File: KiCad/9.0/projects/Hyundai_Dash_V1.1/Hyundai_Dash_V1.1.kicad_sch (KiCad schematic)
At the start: 30 parts, among them J1 +12V-GND, J10 GND-Fuel, J2 IGN-HS1-HS2-LS1-LS2, J3 C-CAN, J4 C-CAN, J5 C-CAN SPI, J6 B-CAN, J7 B-CAN, J8 B-CAN SPI, J9 Jumper Holder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

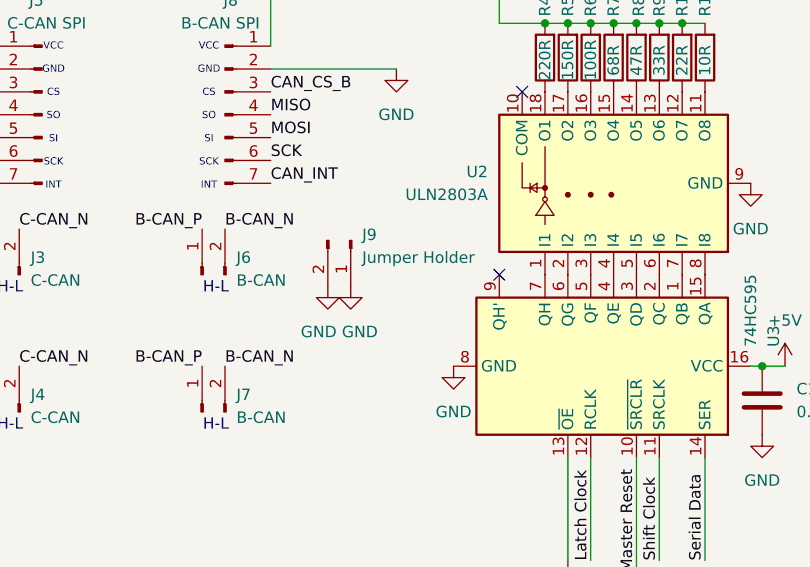
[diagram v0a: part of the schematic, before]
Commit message: KiCad: Hyundai_Dash_V1.1: remove jumper holder
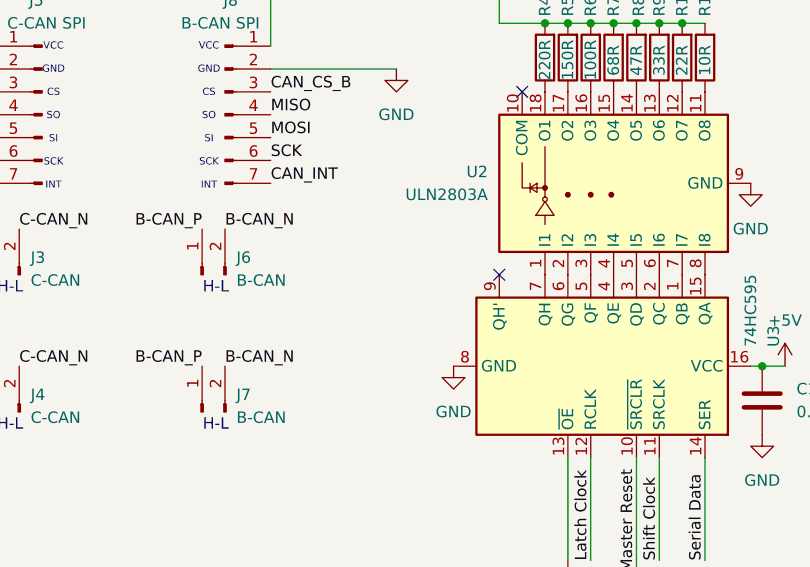
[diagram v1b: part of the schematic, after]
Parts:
- removed J9: Jumper Holder, Connector_PinHeader_2.54mm:PinHeader_1x02_P2.54mm_Vertical, symbol Connector:Conn_01x02_Pin
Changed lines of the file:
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@@
-	)
-	(symbol
-		(lib_id "power:GND")
-		(at 179.07 86.36 0)
-		(unit 1)
-		(exclude_from_sim no)
-		(in_bom yes)
-		(on_board yes)
-		(dnp no)
-		(property "Reference" "#PWR010"
-			(at 179.07 92.71 0)
-			(effects
-				(font
-					(size 1.27 1.27)
-				)
-				(hide yes)
-			)
-		)
-		(property "Value" "GND"
-			(at 180.086 91.44 0)
-			(effects
-				(font
-					(size 1.27 1.27)
-				)
-			)
-		)
-		(property "Footprint" ""
-			(at 179.07 86.36 0)
-			(effects
-				(font
-					(size 1.27 1.27)
-				)
-				(hide yes)
-			)
-		)
-		(property "Datasheet" ""
-			(at 179.07 86.36 0)
-			(effects
-				(font
-					(size 1.27 1.27)
-				)
-				(hide yes)
-			)
-		)
-		(property "Description" "Power symbol creates a global label with name \"GND\" , ground"
-			(at 179.07 86.36 0)
-			(effects
-				(font
-					(size 1.27 1.27)
-				)
-				(hide yes)
-			)
-		)
-		(pin "1"
-		)
-		(instances
-			(project "Kia_Dash_V1"
-				(path "/37058ee5-1984-4ba0-87f5-ec991eadee3c"
-					(reference "#PWR010")
-					(unit 1)
-				)
-			)
-		)
 	)
 	(symbol
@@
 	)
 	(symbol
-		(lib_id "power:GND")
-		(at 176.53 86.36 0)
-		(unit 1)
-		(exclude_from_sim no)
-		(in_bom yes)
-		(on_board yes)
-		(dnp no)
-		(property "Reference" "#PWR09"
-			(at 176.53 92.71 0)
-			(effects
-				(font
-					(size 1.27 1.27)
-				)
-				(hide yes)
-			)
-		)
-		(property "Value" "GND"
-			(at 175.514 91.44 0)
-			(effects
-				(font
-					(size 1.27 1.27)
-				)
-			)
-		)
-		(property "Footprint" ""
-			(at 176.53 86.36 0)
-			(effects
-				(font
-					(size 1.27 1.27)
-				)
-				(hide yes)
-			)
-		)
-		(property "Datasheet" ""
-			(at 176.53 86.36 0)
-			(effects
-				(font
-					(size 1.27 1.27)
-				)
-				(hide yes)
-			)
-		)
-		(property "Description" "Power symbol creates a global label with name \"GND\" , ground"
-			(at 176.53 86.36 0)
-			(effects
-				(font
-					(size 1.27 1.27)
-				)
-				(hide yes)
-			)
-		)
-		(pin "1"
-		)
-		(instances
-			(project "Kia_Dash_V1"
-				(path "/37058ee5-1984-4ba0-87f5-ec991eadee3c"
-					(reference "#PWR09")
-					(unit 1)
-				)
-			)
-		)
-	)
-	(symbol
 		(lib_id "Transistor_Array:ULN2803A")
 		(at 104.14 86.36 90)
@@
 					(unit 1)
 				)
-			)
-		)
-	)
-	(symbol
-		(lib_id "Connector:Conn_01x02_Pin")
-		(at 179.07 81.28 270)
-		(unit 1)
-		(exclude_from_sim no)
-		(in_bom no)
-		(on_board yes)
-		(dnp no)
-		(fields_autoplaced yes)
-		(property "Reference" "J9"
-			(at 180.34 80.6449 90)
-			(effects
-				(font
-					(size 1.27 1.27)
-				)
-				(justify left)
-			)
-		)
-		(property "Value" "Jumper Holder"
-			(at 180.34 83.1849 90)
-			(effects
-				(font
-					(size 1.27 1.27)
-				)
-				(justify left)
-			)
-		)
-		(property "Footprint" "Connector_PinHeader_2.54mm:PinHeader_1x02_P2.54mm_Vertical"
-			(at 179.07 81.28 0)
-			(effects
-				(font
-					(size 1.27 1.27)
-				)
-				(hide yes)
-			)
-		)
-		(property "Datasheet" "~"
-			(at 179.07 81.28 0)
-			(effects
-				(font
-					(size 1.27 1.27)
-				)
-				(hide yes)
-			)
-		)
-		(property "Description" "Generic connector, single row, 01x02, script generated"
-			(at 179.07 81.28 0)
-			(effects
-				(font
-					(size 1.27 1.27)
-				)
-				(hide yes)
-			)
-		)
-		(pin "1"
-		)
-		(pin "2"
-		)
-		(instances
-			(project "Hyundai_Dash_V3"
-				(path "/37058ee5-1984-4ba0-87f5-ec991eadee3c"
-					(reference "J9")
-					(unit 1)
-				)

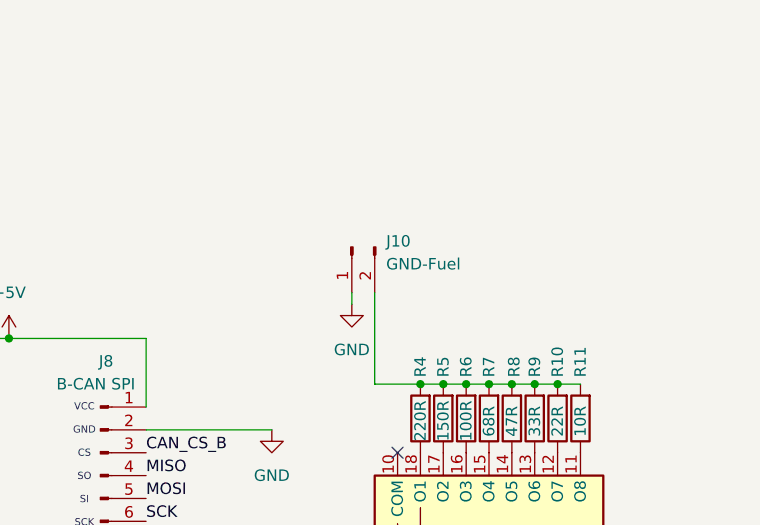
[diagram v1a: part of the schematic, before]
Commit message: KiCad: Hyundai_Dash_V1.1: reassign annotations
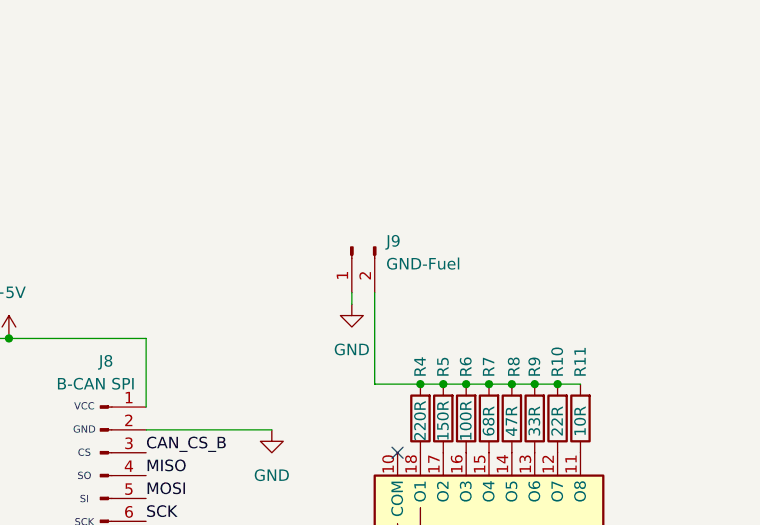
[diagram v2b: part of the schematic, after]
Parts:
- renumbered J10 to J9
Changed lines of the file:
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@@
 		(dnp no)
 		(fields_autoplaced yes)
-		(property "Reference" "#PWR014"
+		(property "Reference" "#PWR012"
 			(at 203.2 123.19 0)
 			(effects
@@
 			(project "Elantra_Nano"
 				(path "/37058ee5-1984-4ba0-87f5-ec991eadee3c"
-					(reference "#PWR014")
+					(reference "#PWR012")
 					(unit 1)
 				)
@@
 		(dnp no)
 		(fields_autoplaced yes)
-		(property "Reference" "J10"
+		(property "Reference" "J9"
 			(at 196.85 41.2749 90)
 			(effects
@@
 			(project "Elantra_Nano"
 				(path "/37058ee5-1984-4ba0-87f5-ec991eadee3c"
-					(reference "J10")
+					(reference "J9")
 					(unit 1)
 				)
@@
 		(dnp no)
 		(fields_autoplaced yes)
-		(property "Reference" "#PWR017"
+		(property "Reference" "#PWR015"
 			(at 227.33 99.06 0)
 			(effects
@@
 			(project "Elantra_Nano"
 				(path "/37058ee5-1984-4ba0-87f5-ec991eadee3c"
-					(reference "#PWR017")
+					(reference "#PWR015")
 					(unit 1)
 				)
@@
 		(dnp no)
 		(fields_autoplaced yes)
-		(property "Reference" "#PWR013"
+		(property "Reference" "#PWR011"
 			(at 193.04 54.61 0)
 			(effects
@@
 			(project "Elantra_Nano"
 				(path "/37058ee5-1984-4ba0-87f5-ec991eadee3c"
-					(reference "#PWR013")
+					(reference "#PWR011")
 					(unit 1)
 				)
@@
 		(dnp no)
 		(fields_autoplaced yes)
-		(property "Reference" "#PWR011"
+		(property "Reference" "#PWR09"
 			(at 184.15 68.58 0)
 			(effects
@@
 			(project "Hyundai_Dash_V3"
 				(path "/37058ee5-1984-4ba0-87f5-ec991eadee3c"
-					(reference "#PWR011")
+					(reference "#PWR09")
 					(unit 1)
 				)
@@
 		(dnp no)
 		(fields_autoplaced yes)
-		(property "Reference" "#PWR012"
+		(property "Reference" "#PWR010"
 			(at 190.5 101.6 0)
 			(effects
@@
 			(project "Elantra_Nano"
 				(path "/37058ee5-1984-4ba0-87f5-ec991eadee3c"
-					(reference "#PWR012")
+					(reference "#PWR010")
 					(unit 1)
 				)
@@
 		(dnp no)
 		(fields_autoplaced yes)
-		(property "Reference" "#PWR015"
+		(property "Reference" "#PWR013"
 			(at 223.52 81.28 0)
 			(effects
@@
 			(project "Elantra_Nano"
 				(path "/37058ee5-1984-4ba0-87f5-ec991eadee3c"
-					(reference "#PWR015")
+					(reference "#PWR013")
 					(unit 1)
 				)
@@
 		(dnp no)
 		(fields_autoplaced yes)
-		(property "Reference" "#PWR016"
+		(property "Reference" "#PWR014"
 			(at 224.79 109.22 0)
 			(effects
@@
 			(project "Elantra_Nano"
 				(path "/37058ee5-1984-4ba0-87f5-ec991eadee3c"
-					(reference "#PWR016")
-					(unit 1)
-				)
+					(reference "#PWR014")
+					(unit 1)
+				)
